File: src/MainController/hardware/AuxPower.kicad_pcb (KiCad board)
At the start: 2 copper layers, 90 x 90 mm, 123 parts, among them J1 MC 1,5/2, J10 MC 1,5/4, J11 S3B-XH-A, J12 S3B-XH-A, J13 S3B-XH-A, J14 S3B-XH-A, J15 S3B-XH-A, J16 B3B-XH-A, J17 B4B-XH-A, J2 MC 1,5/2, J3 MC 1,5/2, J4 MC 1,5/2, J5 MC 1,5/2, J6 MC 1,5/4, J7 MC 1,5/4, J8 MC 1,5/4, J9 MC 1,5/4, Q1 BC846B,235, Q10 RS3L110, Q2 BC846B,235, Q3 BC846B,235, Q4 BC846B,235, Q5 BC846B,235, Q6 RS3L110, Q7 RS3L110, Q8 RS3L110, Q9 RS3L110, U1 ZXCT1009, U2 ZXCT1009, U3 ZXCT1009, U4 ZXCT1009, U5 ZXCT1009, U6 PIC18F26K83, U7 PI4IOE5V6416, U8 MCP9701

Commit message: Updated components to match new ratios
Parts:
- R1, R2, R3, R4, R5: value 0R05 -> 0R025
- R36, R37, R38, R39, R40: value 4K42 -> 6K19
- R41: value 5K6 -> 6K8
- R52: value 39K2 -> 102K
- R58, R59, R60, R61, R62: value 137K -> 390K
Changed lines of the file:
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@@
 			)
 		)
-		(property "Value" "4K42"
+		(property "Value" "6K19"
 			(at 2.3 0 0)
 			(layer "B.SilkS")
@@
 			)
 		)
-		(property "Value" "0R05"
+		(property "Value" "0R025"
 			(at 0 0 90)
 			(layer "B.SilkS")
@@
 			)
 		)
-		(property "Value" "137K"
+		(property "Value" "390K"
 			(at 2.3 0 0)
 			(layer "B.SilkS")
@@
 			)
 		)
-		(property "Value" "137K"
+		(property "Value" "390K"
 			(at 2.3 0 0)
 			(layer "B.SilkS")
@@
 			)
 		)
-		(property "Value" "0R05"
+		(property "Value" "0R025"
 			(at 0 0 90)
 			(layer "B.SilkS")
@@
 			)
 		)
-		(property "Value" "0R05"
+		(property "Value" "0R025"
 			(at 0 0 90)
 			(layer "B.SilkS")
@@
 			)
 		)
-		(property "Value" "137K"
+		(property "Value" "390K"
 			(at 2.3 0 0)
 			(layer "B.SilkS")
@@
 			)
 		)
-		(property "Value" "0R05"
+		(property "Value" "0R025"
 			(at 0 0 90)
 			(layer "B.SilkS")
@@
 			)
 		)
-		(property "Value" "4K42"
+		(property "Value" "6K19"
 			(at 2.3 0 0)
 			(layer "B.SilkS")
@@
 			)
 		)
-		(property "Value" "0R05"
+		(property "Value" "0R025"
 			(at 0 0 90)
 			(layer "B.SilkS")
@@
 			)
 		)
-		(property "Value" "4K42"
+		(property "Value" "6K19"
 			(at 2.3 0 0)
 			(layer "B.SilkS")
@@
 			)
 		)
-		(property "Value" "4K42"
+		(property "Value" "6K19"
 			(at 2.3 0 0)
 			(layer "B.SilkS")
@@
 			)
 		)
-		(property "Value" "137K"
+		(property "Value" "390K"
 			(at 2.3 0 0)
 			(layer "B.SilkS")
@@
 			)
 		)
-		(property "Value" "39K2"
+		(property "Value" "102K"
 			(at 2.3 0 90)
 			(layer "B.SilkS")
@@
 			)
 		)
-		(property "Value" "137K"
+		(property "Value" "390K"
 			(at 2.3 0 0)
 			(layer "B.SilkS")
@@
 			)
 		)
-		(property "Value" "5K6"
+		(property "Value" "6K8"
 			(at -2.3 0 -90)
 			(layer "B.SilkS")
@@
 			)
 		)
-		(property "Value" "4K42"
+		(property "Value" "6K19"
 			(at 2.3 0 0)
 			(layer "B.SilkS")

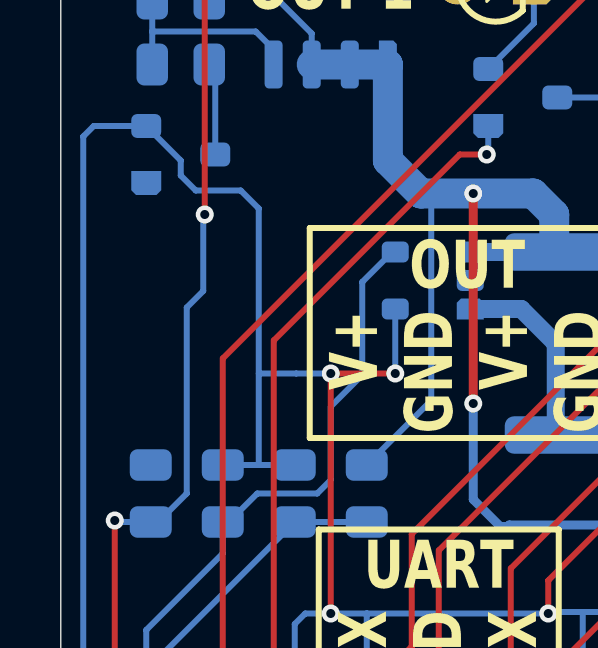
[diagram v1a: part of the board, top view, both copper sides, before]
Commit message: MainController: Added missing trace
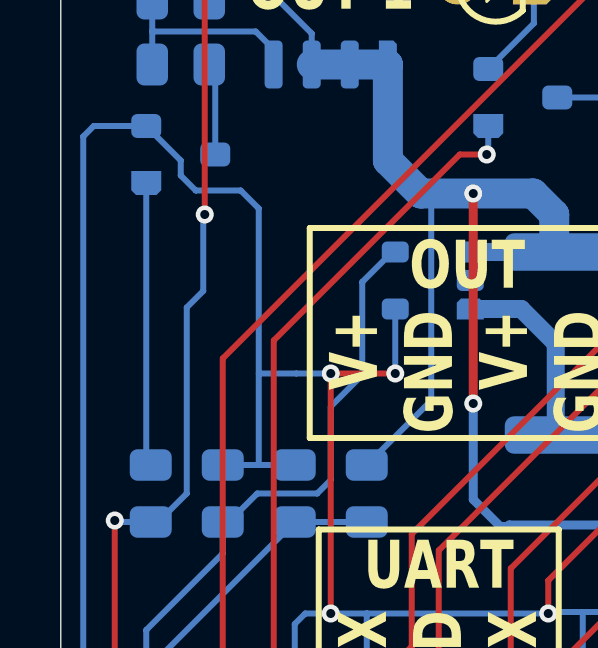
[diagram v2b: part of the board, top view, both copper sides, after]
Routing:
- net BASE1: track 0.00 -> 9.46 mm
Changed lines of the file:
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@@
+	)
+	(segment
+		(start 17.85 44.9)
+		(end 18 45.05)
+		(width 0.2)
+		(layer "B.Cu")
+		(net 21)
+	)
+	(segment
+		(start 17.85 35.65)
+		(end 17.85 44.9)
+		(width 0.2)
+		(layer "B.Cu")
+		(net 21)
 	)
 	(segment

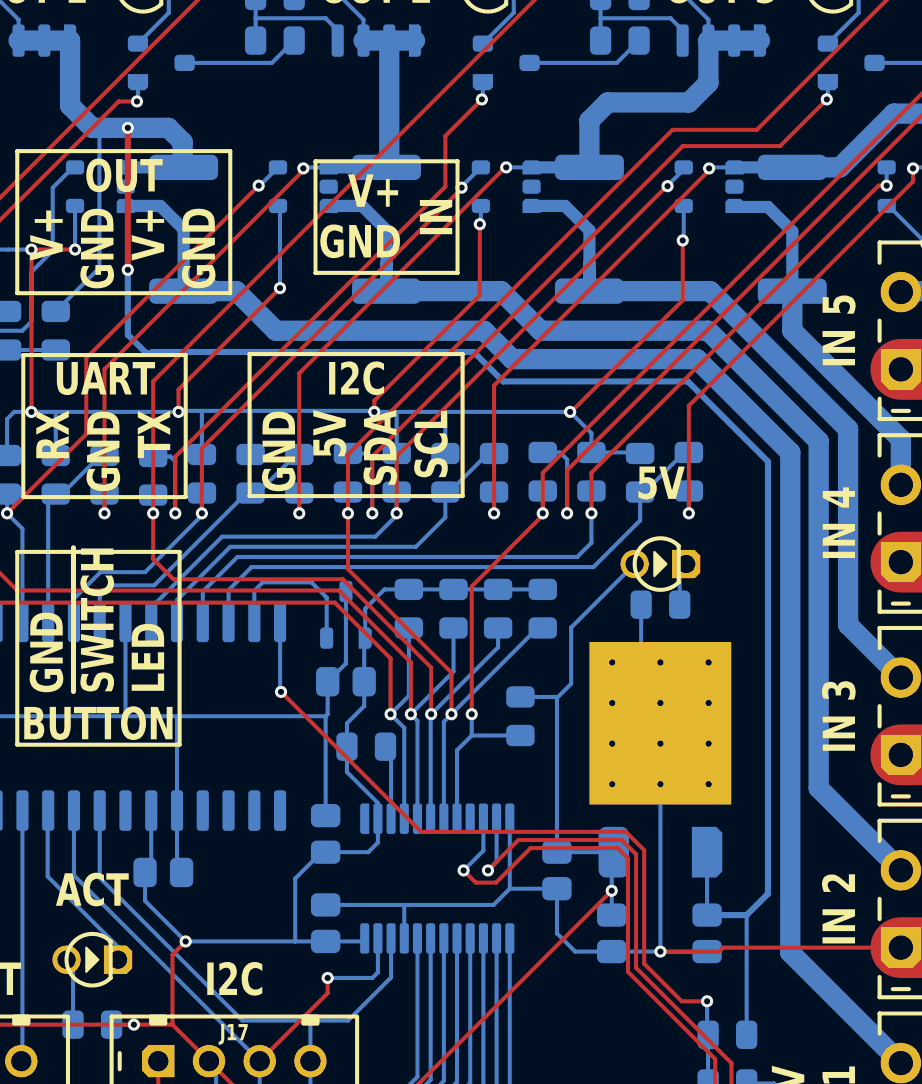
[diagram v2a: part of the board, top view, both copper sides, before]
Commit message: Moved 12V input before sense line
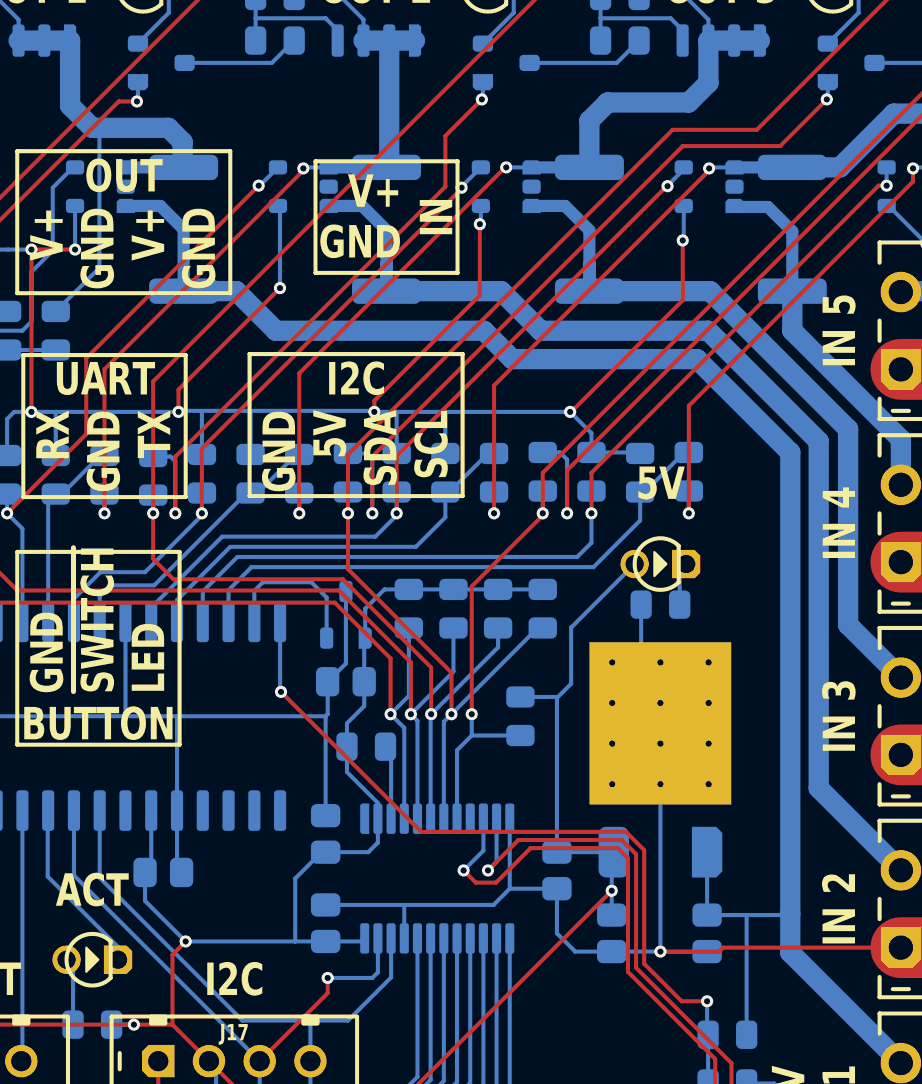
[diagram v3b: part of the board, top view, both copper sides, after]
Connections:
- C7 pad 2: INPUT1' -> INPUT1
- R52 pad 1: INPUT1' -> INPUT1
- VR1 pad 1: INPUT1' -> INPUT1
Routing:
- net INPUT1': track 115.8 -> 35.7 mm, vias 2 -> 0
- net INPUT1: track 71.9 -> 87.0 mm
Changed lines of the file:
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@@
 			(layers "B.Cu" "B.Paste" "B.Mask")
 			(roundrect_rratio 0.25)
-			(net 33 "INPUT1'")
+			(net 32 "INPUT1")
 			(thermal_bridge_angle 45)
 		)
@@
 			(chamfer_ratio 0.2)
 			(chamfer top_left bottom_left)
-			(net 33 "INPUT1'")
+			(net 32 "INPUT1")
 			(thermal_bridge_angle 45)
 		)
@@
 			(layers "B.Cu" "B.Paste" "B.Mask")
 			(roundrect_rratio 0.25)
-			(net 33 "INPUT1'")
+			(net 32 "INPUT1")
 			(thermal_bridge_angle 45)
 		)
@@
 	)
 	(segment
+		(start 57.3 74.8)
+		(end 61.35 74.8)
+		(width 0.2)
+		(layer "B.Cu")
+		(net 32)
+	)
+	(segment
 		(start 61.4 52)
 		(end 56.8 47.4)
@@
 	)
 	(segment
+		(start 61.35 74.8)
+		(end 61.4 74.75)
+		(width 0.2)
+		(layer "B.Cu")
+		(net 32)
+	)
+	(segment
+		(start 61.4 74.75)
+		(end 61.4 52)
+		(width 1)
+		(layer "B.Cu")
+		(net 32)
+	)
+	(segment
+		(start 57.3 74.8)
+		(end 57.3 71.7)
+		(width 0.2)
+		(layer "B.Cu")
+		(net 32)
+	)
+	(segment
+		(start 61.4 76.645)
+		(end 61.4 74.75)
+		(width 1)
+		(layer "B.Cu")
+		(net 32)
+	)
+	(segment
 		(start 30.35 39.85)
 		(end 31.5 41)
@@
 	)
 	(segment
-		(start 61.4 76.645)
-		(end 61.4 52)
-		(width 1)
+		(start 59.25 80.7)
+		(end 59.25 74.8)
+		(width 0.2)
 		(layer "B.Cu")
 		(net 32)
@@
 	)
 	(segment
-		(start 28.75 43)
-		(end 28.75 36)
-		(width 0.3)
-		(layer "F.Cu")
-		(net 33)
-	)
-	(via
-		(at 28.75 36)
-		(size 0.6)
-		(drill 0.3)
-		(layers "F.Cu" "B.Cu")
-		(net 33)
-	)
-	(via
-		(at 28.75 43)
-		(size 0.6)
-		(drill 0.3)
-		(layers "F.Cu" "B.Cu")
-		(net 33)
-	)
-	(segment
-		(start 60.3 73.75)
-		(end 60.3 52.45)
-		(width 0.3)
-		(layer "B.Cu")
-		(net 33)
-	)
-	(segment
-		(start 45.8 47.05)
-		(end 29.95 47.05)
-		(width 0.3)
-		(layer "B.Cu")
-		(net 33)
-	)
-	(segment
-		(start 29.65 47.1)
-		(end 28.75 46.2)
-		(width 0.3)
-		(layer "B.Cu")
-		(net 33)
-	)
-	(segment
-		(start 57.3 74.8)
-		(end 57.3 71.7)
-		(width 0.2)
-		(layer "B.Cu")
-		(net 33)
-	)
-	(segment
-		(start 60.3 52.45)
-		(end 56.35 48.5)
-		(width 0.3)
-		(layer "B.Cu")
-		(net 33)
-	)
-	(segment
-		(start 59.25 80.7)
-		(end 59.25 74.8)
+		(start 59.25 74.8)
+		(end 57.3 74.8)
 		(width 0.2)
 		(layer "B.Cu")
-		(net 33)
+		(net 32)
 	)
 	(segment
@@
 	)
 	(segment
-		(start 59.25 74.8)
-		(end 60.3 73.75)
-		(width 0.3)
-		(layer "B.Cu")
-		(net 33)
-	)
-	(segment
 		(start 24.635 31.7)
 		(end 23.365 31.7)
@@
 	)
 	(segment
-		(start 47.25 48.5)
-		(end 45.8 47.05)
-		(width 0.3)
-		(layer "B.Cu")
-		(net 33)
-	)
-	(segment
-		(start 59.25 74.8)
-		(end 57.3 74.8)
-		(width 0.3)
-		(layer "B.Cu")
-		(net 33)
-	)
-	(segment
 		(start 30.75 36)
 		(end 31.45 36.7)
@@
 	)
 	(segment
-		(start 28.75 46.2)
-		(end 28.75 43)
-		(width 0.3)
-		(layer "B.Cu")
-		(net 33)
-	)
-	(segment
-		(start 56.35 48.5)
-		(end 47.25 48.5)
-		(width 0.3)
-		(layer "B.Cu")
-		(net 33)
-	)
-	(segment
 		(start 27.35 42.9)
 		(end 27.35 36.2)
@@
 	)
 	(segment
-		(start 29.9 47.1)
-		(end 29.65 47.1)
-		(width 0.3)
-		(layer "B.Cu")
-		(net 33)
-	)
-	(segment
 		(start 31.5 37.95)
 		(end 28.65 37.95)
@@
 		(layer "B.Cu")
 		(net 33)
-	)
-	(segment
-		(start 30.75 36)
-		(end 28.75 36)
-		(width 0.3)
-		(layer "B.Cu")
-		(net 33)
-	)
-	(segment
-		(start 29.95 47.05)
-		(end 29.9 47.1)
-		(width 0.3)
-		(layer "B.Cu")
-		(net 33)

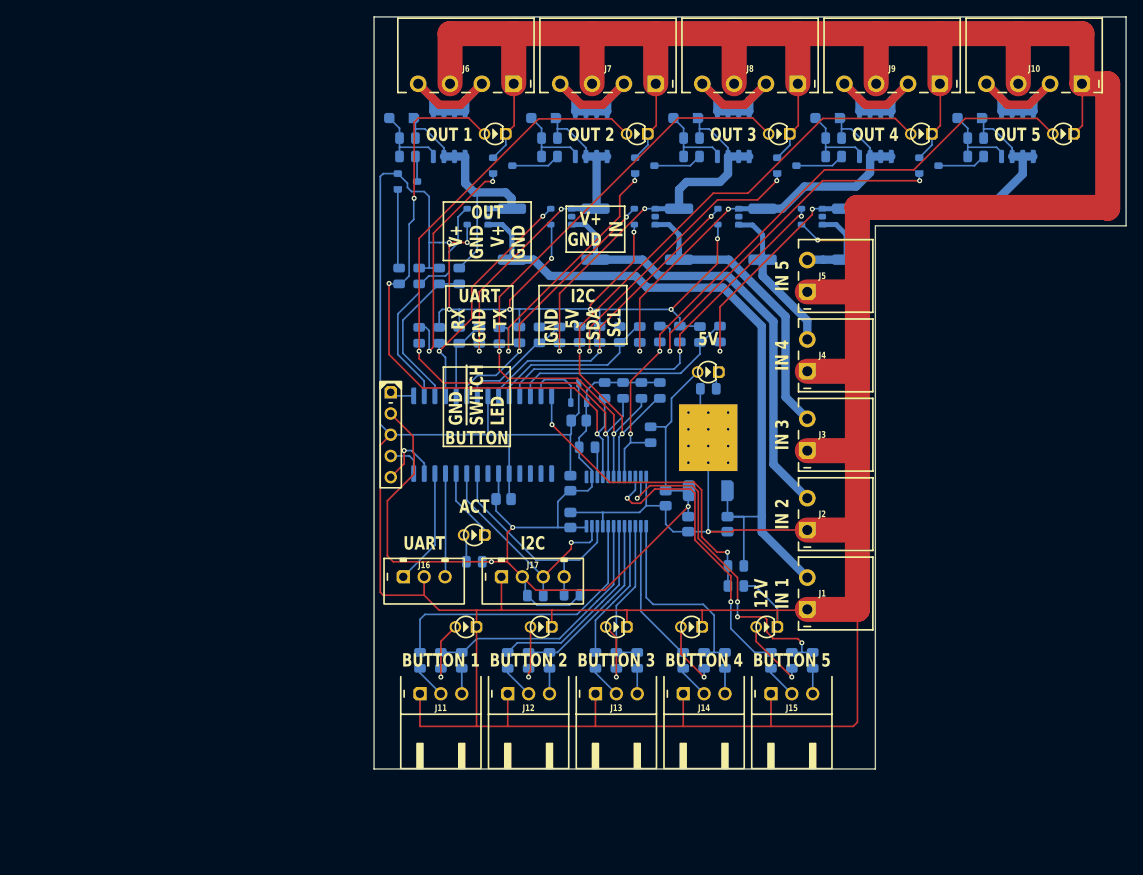
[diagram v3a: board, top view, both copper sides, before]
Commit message: Increased trace width for power
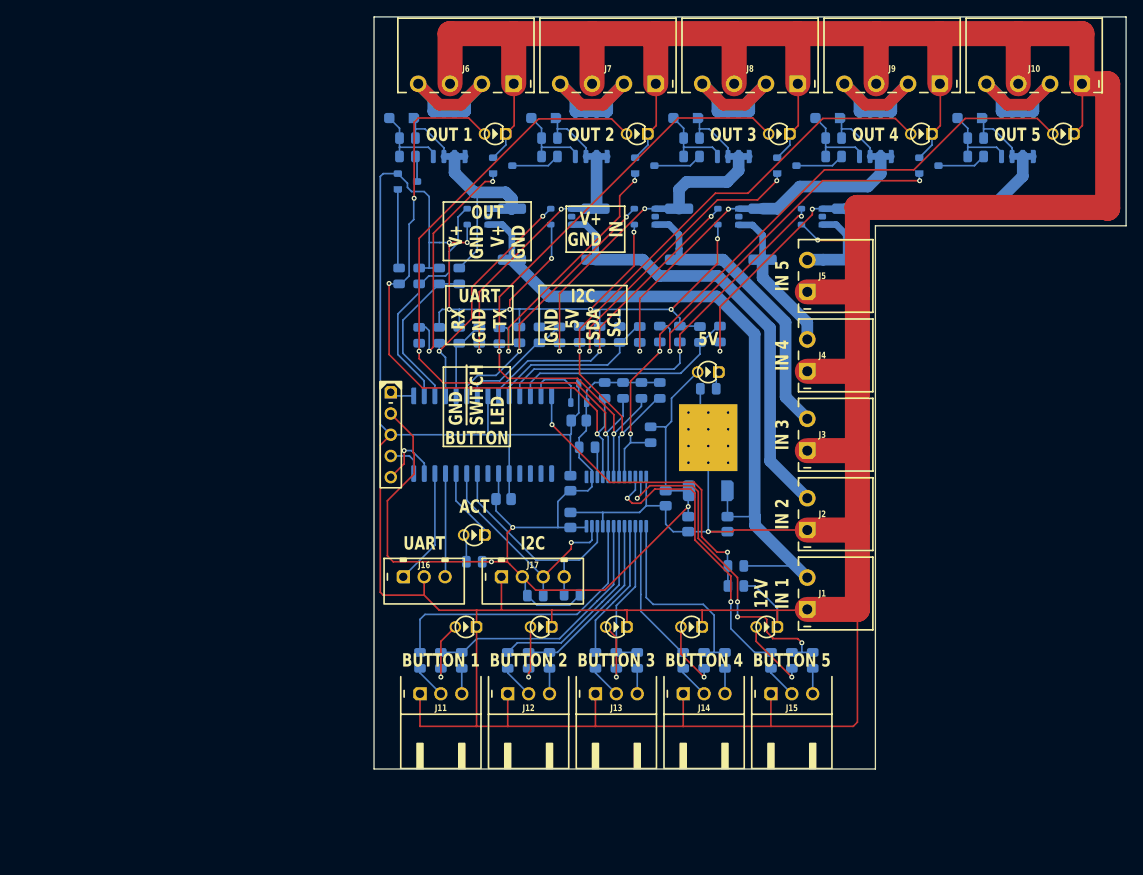
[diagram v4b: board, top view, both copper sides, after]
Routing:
- net INPUT1: track 87.0 -> 85.4 mm
- net INPUT4': track 53.4 -> 54.7 mm
- net INPUT3': track 47.7 -> 48.8 mm
- net ADC_CURRENT5: track 46.5 -> 47.5 mm
- net INPUT2: track 54.4 -> 53.7 mm
- net INPUT1': track 35.7 -> 36.2 mm

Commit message: MainController: wider GND traces
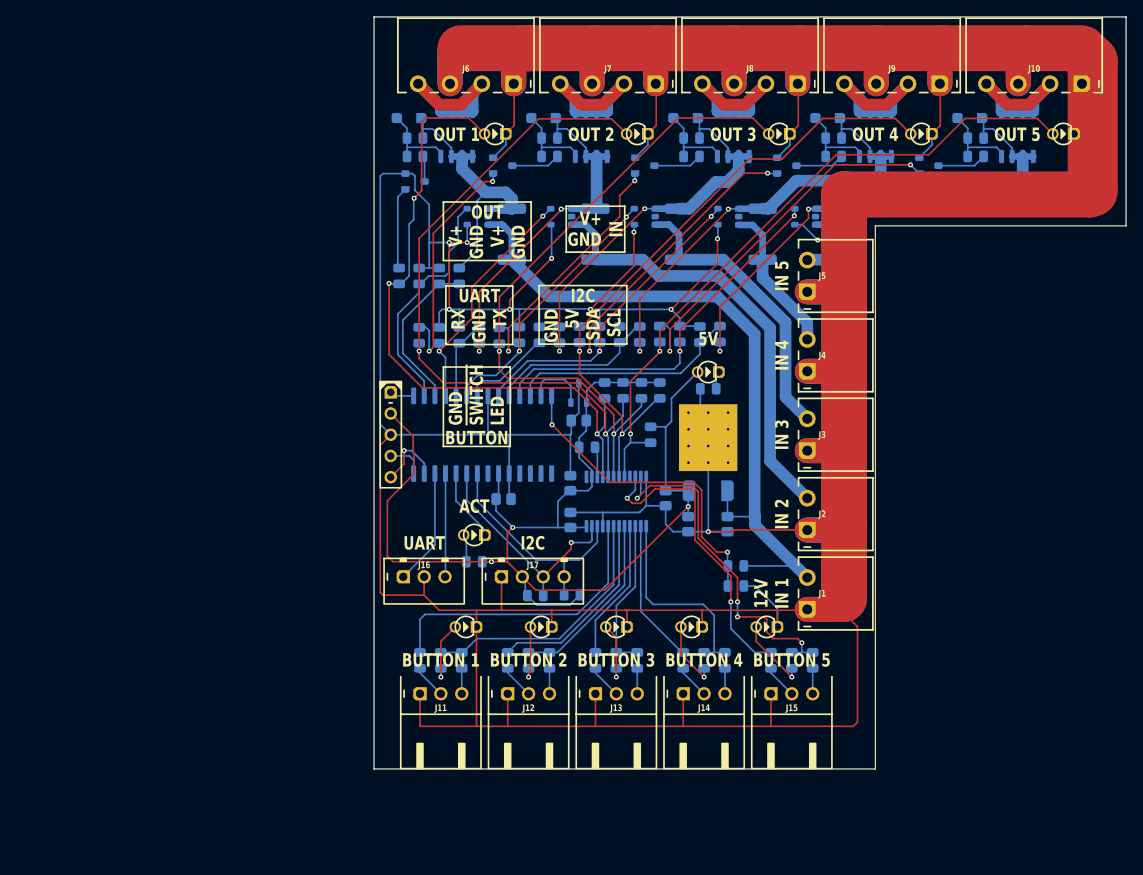
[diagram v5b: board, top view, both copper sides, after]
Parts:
- moved D1 0.90 mm to (19.2, 27.1)
- moved Q1 0.90 mm to (19.9, 34.7)
- moved Q6 0.90 mm to (24.9, 29.0)
- moved R47 0.90 mm to (19.9, 31.7)
- moved R53 0.90 mm to (19.9, 29.5)
- moved U5 0.80 mm to (66.6, 38.9)
- moved R5 0.80 mm to (70.7, 41.0)
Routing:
- net GND: track 776.8 -> 924.7 mm
- net INPUT5': track 62.1 -> 63.6 mm
- net INPUT3': track 48.8 -> 47.4 mm
- net BASE5: track 44.7 -> 45.2 mm
- net ADC_CURRENT5: track 47.5 -> 46.9 mm
- net INPUT1': track 36.2 -> 35.7 mm
- net OUT_OUTPUT1: track 79.6 -> 79.1 mm
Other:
- board text added: "1"
- board text added: "2"
- board text added: "3"
- board text added: "4"
- board text added: "5"

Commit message: Adjusted ADC resistors
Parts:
- R16: value 1K -> 3K3
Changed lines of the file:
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@@
 			)
 		)
-		(property "Value" "1K"
+		(property "Value" "3K3"
 			(at -2.4 -0.1 180)
 			(layer "B.SilkS")
